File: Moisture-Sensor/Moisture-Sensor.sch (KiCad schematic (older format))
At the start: 0 parts

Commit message: Selected most of the required components
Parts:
- added C?: 0.1 uF, Capacitor_SMD:C_0603_1608Metric_Pad1.05x0.95mm_HandSolder, symbol Device:C
- added D?: LED, LED_SMD:LED_0603_1608Metric_Pad1.05x0.95mm_HandSolder, symbol Device:LED
- added J?: Input, Connector_PinSocket_2.54mm:PinSocket_1x03_P2.54mm_Vertical, symbol Connector_Generic:Conn_01x03
- added R? (x2): R, Resistor_SMD:R_0603_1608Metric_Pad1.05x0.95mm_HandSolder, symbol Device:R
- added U?: NE555, Package_SO:SOIC-8-1EP_3.9x4.9mm_P1.27mm_EP2.41x3.81mm, symbol Timer:NE555
- added U? (x2): LMV358, symbol Amplifier_Operational:LMV358
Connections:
- net labels added: +3.3V, GND, Sig
- wire segments 0 -> 6
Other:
- note added: "Need higher input votlage than 3.3"
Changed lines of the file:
@@
 encoding utf-8
 Sheet 1 1
-Title ""
+Title "Capacitance Moisture Sensor"
 Date "2020-12-27"
 Rev "A"
-Comp ""
-Comment1 ""
-Comment2 ""
+Comp "Mark Sherstan"
+Comment1 "All capacitors should be ceramic X7R"
+Comment2 "Manufactured PCB should be sealed in epoxy"
 Comment3 ""
 Comment4 ""
 $EndDescr
+$Comp
+L Device:R R?
+U 1 1 5FE8F3C9
+P 1550 2350
+F 0 "R?" V 1757 2350 50  0000 C CNN
+F 1 "R" V 1666 2350 50  0000 C CNN
+F 2 "Resistor_SMD:R_0603_1608Metric_Pad1.05x0.95mm_HandSolder" V 1480 2350 50  0001 C CNN
+F 3 "~" H 1550 2350 50  0001 C CNN
+	1    1550 2350
+	0    -1   -1   0
+$EndComp
+$Comp
+L Device:LED D?
+U 1 1 5FE8F924
+P 2250 2350
+F 0 "D?" H 2243 2095 50  0000 C CNN
+F 1 "LED" H 2243 2186 50  0000 C CNN
+F 2 "LED_SMD:LED_0603_1608Metric_Pad1.05x0.95mm_HandSolder" H 2250 2350 50  0001 C CNN
+F 3 "~" H 2250 2350 50  0001 C CNN
+	1    2250 2350
+	-1   0    0    1
+$EndComp
+$Comp
+L power:+3.3V #PWR?
+U 1 1 5FE8FE6D
+P 1000 2350
+F 0 "#PWR?" H 1000 2200 50  0001 C CNN
+F 1 "+3.3V" H 1015 2523 50  0000 C CNN
+F 2 "" H 1000 2350 50  0001 C CNN
+F 3 "" H 1000 2350 50  0001 C CNN
+	1    1000 2350
+	1    0    0    -1
+$EndComp
+$Comp
+L power:GND #PWR?
+U 1 1 5FE903CE
+P 2800 2350
+F 0 "#PWR?" H 2800 2100 50  0001 C CNN
+F 1 "GND" H 2805 2177 50  0000 C CNN
+F 2 "" H 2800 2350 50  0001 C CNN
+F 3 "" H 2800 2350 50  0001 C CNN
+	1    2800 2350
+	1    0    0    -1
+$EndComp
+Wire Wire Line
+	1000 2350 1400 2350
+Wire Wire Line
+	1700 2350 2100 2350
+Wire Wire Line
+	2400 2350 2800 2350
+$Comp
+L Connector_Generic:Conn_01x03 J?
+U 1 1 5FE95D2E
+P 1650 1250
+F 0 "J?" H 1568 925 50  0000 C CNN
+F 1 "Input" H 1568 1016 50  0000 C CNN
+F 2 "Connector_PinSocket_2.54mm:PinSocket_1x03_P2.54mm_Vertical" H 1650 1250 50  0001 C CNN
+F 3 "~" H 1650 1250 50  0001 C CNN
+	1    1650 1250
+	-1   0    0    1
+$EndComp
+Text GLabel 2000 1150 2    50   Input ~ 0
+Sig
+$Comp
+L power:GND #PWR?
+U 1 1 5FE9738F
+P 2000 1350
+F 0 "#PWR?" H 2000 1100 50  0001 C CNN
+F 1 "GND" H 2005 1177 50  0000 C CNN
+F 2 "" H 2000 1350 50  0001 C CNN
+F 3 "" H 2000 1350 50  0001 C CNN
+	1    2000 1350
+	1    0    0    -1
+$EndComp
+$Comp
+L power:+3.3V #PWR?
+U 1 1 5FE97B90
+P 2300 1250
+F 0 "#PWR?" H 2300 1100 50  0001 C CNN
+F 1 "+3.3V" H 2315 1423 50  0000 C CNN
+F 2 "" H 2300 1250 50  0001 C CNN
+F 3 "" H 2300 1250 50  0001 C CNN
+	1    2300 1250
+	1    0    0    -1
+$EndComp
+Wire Wire Line
+	1850 1150 2000 1150
+Wire Wire Line
+	1850 1250 2300 1250
+Wire Wire Line
+	1850 1350 2000 1350
+$Comp
+L Timer:NE555 U?
+U 1 1 5FEA5580
+P 4900 2650
+F 0 "U?" H 4900 3231 50  0000 C CNN
+F 1 "NE555" H 4900 3140 50  0000 C CNN
+F 2 "Package_SO:SOIC-8-1EP_3.9x4.9mm_P1.27mm_EP2.41x3.81mm" H 4900 2650 50  0001 C CNN
+F 3 "" H 4900 2650 50  0001 C CNN
+F 4 "Texas Instruments" H 4900 2650 50  0001 C CNN "Manufacturer"
+F 5 "NE555DR" H 4900 2650 50  0001 C CNN "Manufacturer #"
+F 6 "296-6501-1-ND" H 4900 2650 50  0001 C CNN "Digi-Key #"
+F 7 "https://www.digikey.ca/en/products/detail/texas-instruments/NE555DR/372491" H 4900 2650 50  0001 C CNN "Digi-Key LinkDigi LinkDigi-Key Link"
+	1    4900 2650
+	1    0    0    -1
+$EndComp
+$Comp
+L Device:C C?
+U 1 1 5FEA618B
+P 7300 2650
+F 0 "C?" H 7415 2696 50  0000 L CNN
+F 1 "0.1 uF" H 7415 2605 50  0000 L CNN
+F 2 "Capacitor_SMD:C_0603_1608Metric_Pad1.05x0.95mm_HandSolder" H 7338 2500 50  0001 C CNN
+F 3 "~" H 7300 2650 50  0001 C CNN
+	1    7300 2650
+	1    0    0    -1
+$EndComp
+Text Notes 4250 3850 0    50   ~ 0
+Need higher input votlage than 3.3
+$Comp
+L Amplifier_Operational:LMV358 U?
+U 1 1 5FEA7DEB
+P 7000 4600
+F 0 "U?" H 7000 4967 50  0000 C CNN
+F 1 "LMV358" H 7000 4876 50  0000 C CNN
+F 2 "" H 7000 4600 50  0001 C CNN
+F 3 "http://www.ti.com/lit/ds/symlink/lmv324.pdf" H 7000 4600 50  0001 C CNN
+	1    7000 4600
+	1    0    0    -1
+$EndComp
+$Comp
+L Amplifier_Operational:LMV358 U?
+U 3 1 5FEAA329
+P 8200 4600
+F 0 "U?" H 8158 4646 50  0000 L CNN
+F 1 "LMV358" H 8158 4555 50  0000 L CNN
+F 2 "" H 8200 4600 50  0001 C CNN
+F 3 "http://www.ti.com/lit/ds/symlink/lmv324.pdf" H 8200 4600 50  0001 C CNN
+	3    8200 4600
+	1    0    0    -1
+$EndComp
+$Comp
+L Device:R R?
+U 1 1 5FEC3053
+P 7050 1900
+F 0 "R?" V 7257 1900 50  0000 C CNN
+F 1 "R" V 7166 1900 50  0000 C CNN
+F 2 "Resistor_SMD:R_0603_1608Metric_Pad1.05x0.95mm_HandSolder" V 6980 1900 50  0001 C CNN
+F 3 "~" H 7050 1900 50  0001 C CNN
+	1    7050 1900
+	0    -1   -1   0
+$EndComp
 $EndSCHEMATC

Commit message: 555 timer complete
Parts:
- removed U?: NE555, Package_SO:SOIC-8-1EP_3.9x4.9mm_P1.27mm_EP2.41x3.81mm, symbol Timer:NE555
- added C?: 470 pF, Capacitor_SMD:C_0603_1608Metric_Pad1.05x0.95mm_HandSolder, symbol Device:C
- added C?: 10 nF, Capacitor_SMD:C_0603_1608Metric_Pad1.05x0.95mm_HandSolder, symbol Device:C
- added R?: 2.4 kohm, Resistor_SMD:R_0603_1608Metric_Pad1.05x0.95mm_HandSolder, symbol Device:R
- added R?: 10 kohm, Resistor_SMD:R_0603_1608Metric_Pad1.05x0.95mm_HandSolder, symbol Device:R
- added U?: LM555, symbol Custom:LM555
- R?: value R -> 1.5 kohm
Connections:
- net labels added: +5V
- wire segments 6 -> 32
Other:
- note removed: "Need higher input votlage than 3.3"
- moved on the sheet: C?, D?, J?, R?, U?C

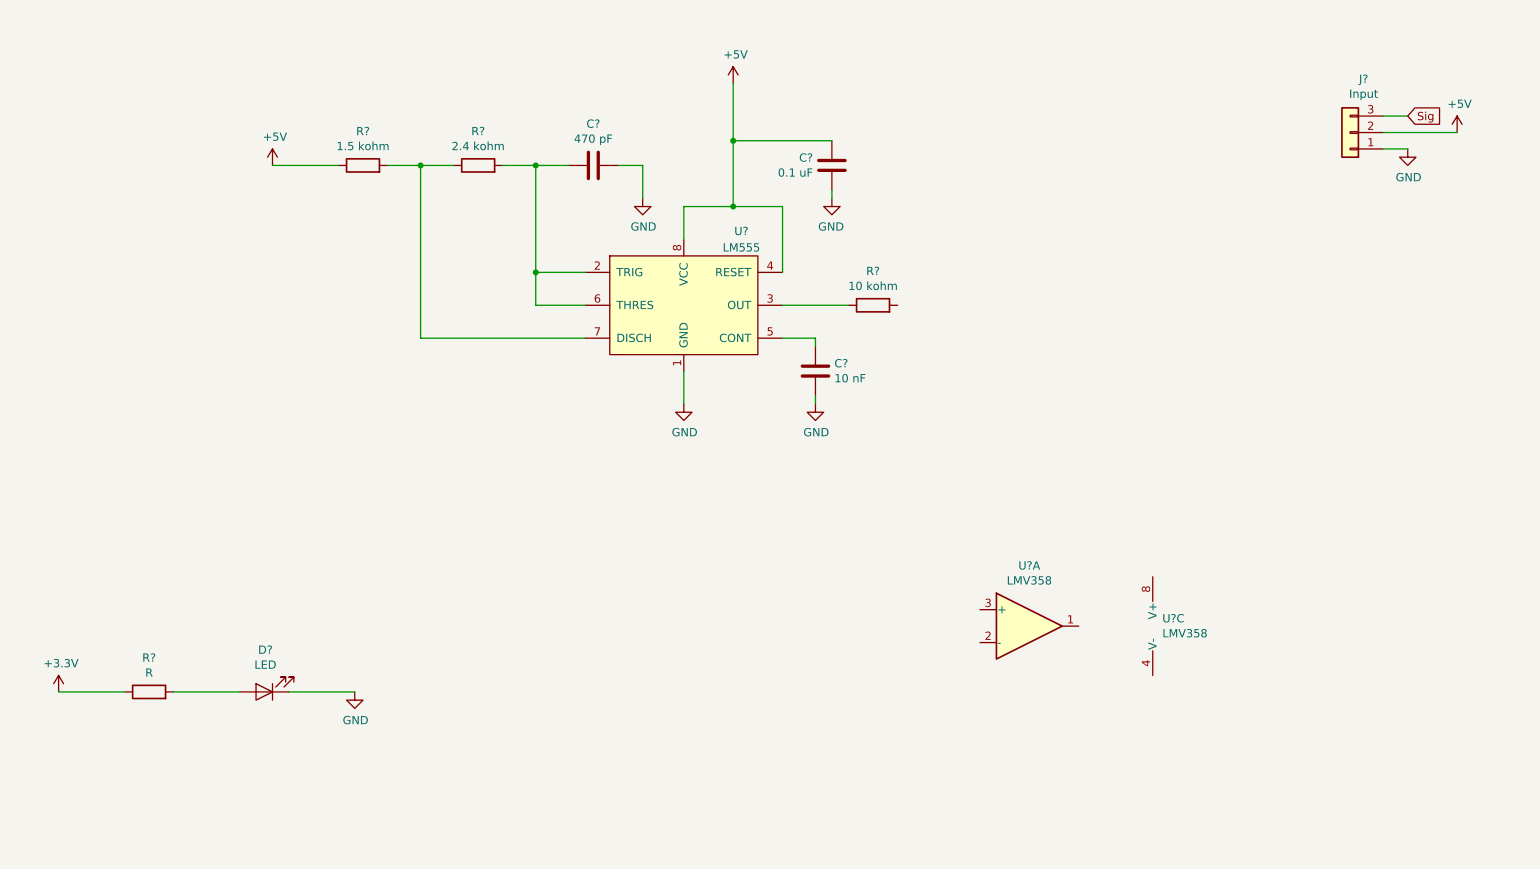
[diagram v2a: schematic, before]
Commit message: Op amp is updated
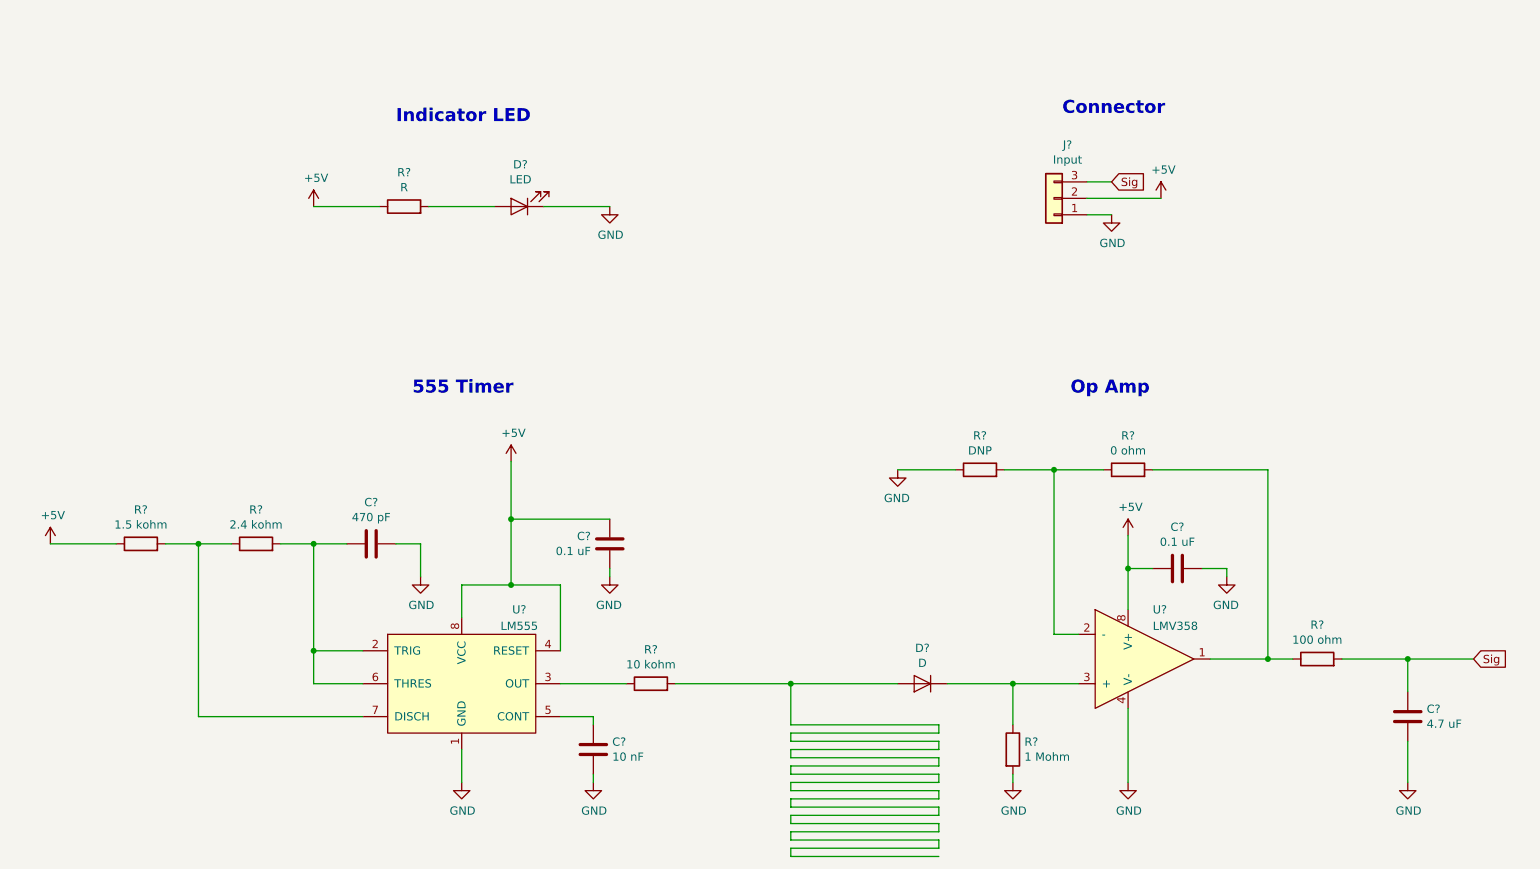
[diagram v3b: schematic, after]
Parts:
- removed U? (x2): LMV358, symbol Amplifier_Operational:LMV358
- added C?: 4.7 uF, Capacitor_SMD:C_0603_1608Metric_Pad1.05x0.95mm_HandSolder, symbol Device:C
- added C?: 0.1 uF, Capacitor_SMD:C_0603_1608Metric_Pad1.05x0.95mm_HandSolder, symbol Device:C
- added D?: D, symbol Device:D
- added R?: 100 ohm, Resistor_SMD:R_0603_1608Metric_Pad1.05x0.95mm_HandSolder, symbol Device:R
- added R?: 0 ohm, Resistor_SMD:R_0603_1608Metric_Pad1.05x0.95mm_HandSolder, symbol Device:R
- added R?: DNP, Resistor_SMD:R_0603_1608Metric_Pad1.05x0.95mm_HandSolder, symbol Device:R
- added R?: 1 Mohm, Resistor_SMD:R_0603_1608Metric_Pad1.05x0.95mm_HandSolder, symbol Device:R
- added U?: LMV358, symbol Custom:LMV358
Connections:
- net +3V3 is gone; now on net +5V: R?.1
- net +5V: now also C?.2, U?.8 (V+)
- net GND: now also C?.1, C?.1, R?.1, R?.2, U?.4 (V-)
- net Sig: now also C?.2, R?.2
- net at R?.2: now also D?.2 (A)
- new net: R?.1, R?.2, U?.1
- new net: R?.1, R?.2, U?.2 (-)
- new net: D?.1 (K), R?.1, U?.3 (+)
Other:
- note added: "555 Timer"
- note added: "Connector"
- note added: "Indicator LED"
- note added: "Op Amp"
- moved on the sheet: C?, D?, J?, R?, U?

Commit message: Schematic just needs a double check
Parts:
- removed U?: LM555, symbol Custom:LM555
- added U2: NE555, Package_SO:SOIC-8_3.9x4.9mm_P1.27mm, symbol Custom:NE555
- D2: renamed from D?; value D -> 4148; footprint (none) -> Diode_SMD:D_SOD-123; Digi-Key # (none) -> SMMSD4148T3GOSCT-ND; Digi-Key LinkDigi LinkDigi-Key Link (none) -> https://www.digikey.ca/en/products/detail/on-semiconductor/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; Manufacturer (none) -> ON Semiconductor; Manufacturer # (none) -> SMMSD4148T3G
- U1: renamed from U?; footprint (none) -> Package_SO:SOIC-8_3.9x4.9mm_P1.27mm; Digi-Key # (none) -> 296-39049-5-ND; Digi-Key LinkDigi LinkDigi-Key Link (none) -> https://www.digikey.ca/en/products/detail/texas-instruments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; Manufacturer (none) -> Texas Instruments; Manufacturer # (none) -> LMV358ID
- gave numbers to parts that had none: 15
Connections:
- net +5V: now also U2.4 (RESET), U2.8 (VCC)
- net GND: now also U2.1 (GND)
- net at R4.2, R5.1: now also U2.7 (DISCH)
- net at C1.2, R5.2: now also U2.2 (TRIG), U2.6 (THRES)
- net at C4.2: now also U2.5 (CONT)
- net at R7.1: now also U2.3 (OUT)
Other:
- moved on the sheet: C5, R6

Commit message: Schematic reviewed
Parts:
- D1: value LED -> Green 2.2V 20mA
- J1: footprint Connector_PinSocket_2.54mm:PinSocket_1x03_P2.54mm_Vertical -> Connector_PinHeader_2.54mm:PinHeader_1x03_P2.54mm_Vertical
- R1: value R -> 150 ohm
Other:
- note added: "Capacitor Trace"
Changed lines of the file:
@@
 EESchema Schematic File Version 4
+LIBS:Moisture-Sensor-cache
 EELAYER 30 0
 EELAYER END
@@
 Sheet 1 1
 Title "Capacitance Moisture Sensor"
-Date "2020-12-27"
+Date "2020-12-28"
 Rev "A"
 Comp "Mark Sherstan"
-Comment1 "All capacitors should be ceramic X7R"
-Comment2 "Manufactured PCB should be sealed in epoxy"
-Comment3 ""
+Comment1 "Capacitors should be ceramic 16V 10% X7R "
+Comment2 "Resistors should be 1/10W 5%"
+Comment3 "Manufactured PCB should be sealed in epoxy"
 Comment4 ""
 $EndDescr
@@
 P 3200 2050
 F 0 "R1" V 3407 2050 50  0000 C CNN
-F 1 "R" V 3316 2050 50  0000 C CNN
+F 1 "150 ohm" V 3316 2050 50  0000 C CNN
 F 2 "Resistor_SMD:R_0603_1608Metric_Pad1.05x0.95mm_HandSolder" V 3130 2050 50  0001 C CNN
 F 3 "~" H 3200 2050 50  0001 C CNN
@@
 P 3900 2050
 F 0 "D1" H 3893 1795 50  0000 C CNN
-F 1 "LED" H 3893 1886 50  0000 C CNN
+F 1 "Green 2.2V 20mA" H 3893 1886 50  0000 C CNN
 F 2 "LED_SMD:LED_0603_1608Metric_Pad1.05x0.95mm_HandSolder" H 3900 2050 50  0001 C CNN
 F 3 "~" H 3900 2050 50  0001 C CNN
@@
 F 0 "J1" H 7068 1675 50  0000 C CNN
 F 1 "Input" H 7068 1766 50  0000 C CNN
-F 2 "Connector_PinSocket_2.54mm:PinSocket_1x03_P2.54mm_Vertical" H 7150 2000 50  0001 C CNN
+F 2 "Connector_PinHeader_2.54mm:PinHeader_1x03_P2.54mm_Vertical" H 7150 2000 50  0001 C CNN
 F 3 "~" H 7150 2000 50  0001 C CNN
 	1    7150 2000
@@
 Wire Wire Line
 	4150 4950 4550 4950
-Wire Wire Line
-	5550 5200 6450 5200
-Wire Wire Line
-	6450 5200 6450 5250
-Wire Wire Line
-	6450 5250 5550 5250
-Wire Wire Line
-	5550 5250 5550 5300
-Wire Wire Line
-	5550 5300 6450 5300
-Wire Wire Line
-	6450 5300 6450 5350
-Wire Wire Line
-	6450 5350 5550 5350
-Wire Wire Line
-	5550 5350 5550 5400
-Wire Wire Line
-	5550 5400 6450 5400
-Wire Wire Line
-	6450 5400 6450 5450
-Wire Wire Line
-	6450 5450 5550 5450
-Wire Wire Line
-	5550 5450 5550 5500
-Wire Wire Line
-	5550 5500 6450 5500
-Wire Wire Line
-	6450 5500 6450 5550
-Wire Wire Line
-	6450 5550 5550 5550
-Wire Wire Line
-	5550 5550 5550 5600
-Wire Wire Line
-	5550 5600 6450 5600
-Wire Wire Line
-	6450 5600 6450 5650
-Wire Wire Line
-	6450 5650 5550 5650
-Wire Wire Line
-	5550 5650 5550 5700
-Wire Wire Line
-	5550 5700 6450 5700
-Wire Wire Line
-	6450 5700 6450 5750
-Wire Wire Line
-	6450 5750 5550 5750
-Wire Wire Line
-	5550 5750 5550 5800
-Wire Wire Line
-	5550 5800 6450 5800
-Wire Wire Line
-	6450 5800 6450 5850
-Wire Wire Line
-	6450 5850 5550 5850
-Wire Wire Line
-	5550 5850 5550 5900
-Wire Wire Line
-	5550 5900 6450 5900
-Wire Wire Line
-	6450 5900 6450 5950
-Wire Wire Line
-	6450 5950 5550 5950
-Wire Wire Line
-	5550 5950 5550 6000
-Wire Wire Line
-	5550 6000 6450 6000
-Wire Wire Line
-	4850 4950 5550 4950
-Wire Wire Line
-	5550 4950 5550 5200
-Connection ~ 5550 4950
-Wire Wire Line
-	5550 4950 6200 4950
 Text Notes 3150 1550 0    79   ~ 16
 Indicator LED
@@
 Wire Wire Line
 	8450 3650 7750 3650
+Wire Wire Line
+	4850 4950 6200 4950
+Wire Notes Line
+	5200 4700 5200 5200
+Wire Notes Line
+	5200 5200 5950 5200
+Wire Notes Line
+	5950 5200 5950 4700
+Wire Notes Line
+	5950 4700 5200 4700
+Text Notes 5250 4650 0    50   ~ 0
+Capacitor Trace
 $EndSCHEMATC
